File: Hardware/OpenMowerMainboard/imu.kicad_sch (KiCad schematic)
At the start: 6 parts, among them J20 Conn_01x10_Female

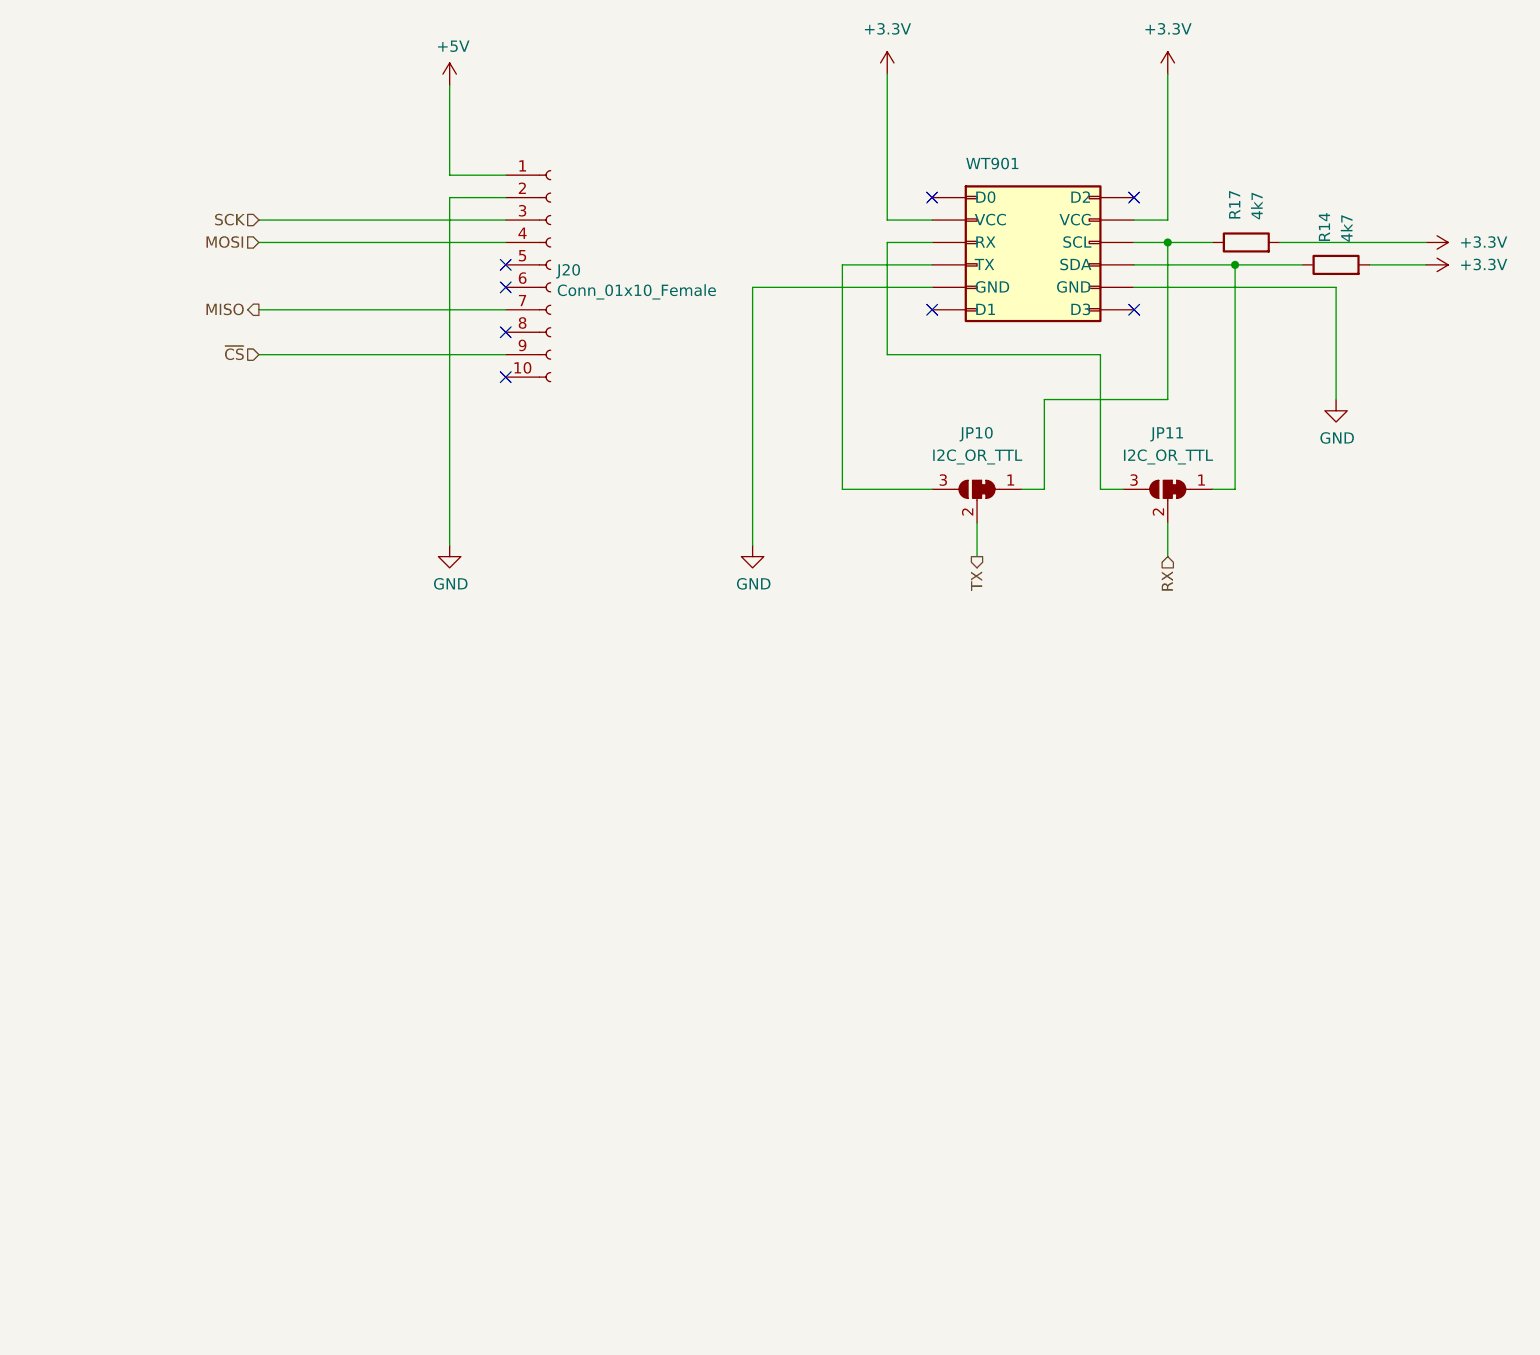
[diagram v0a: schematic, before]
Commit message: feat: added LSM6DSO as IMU
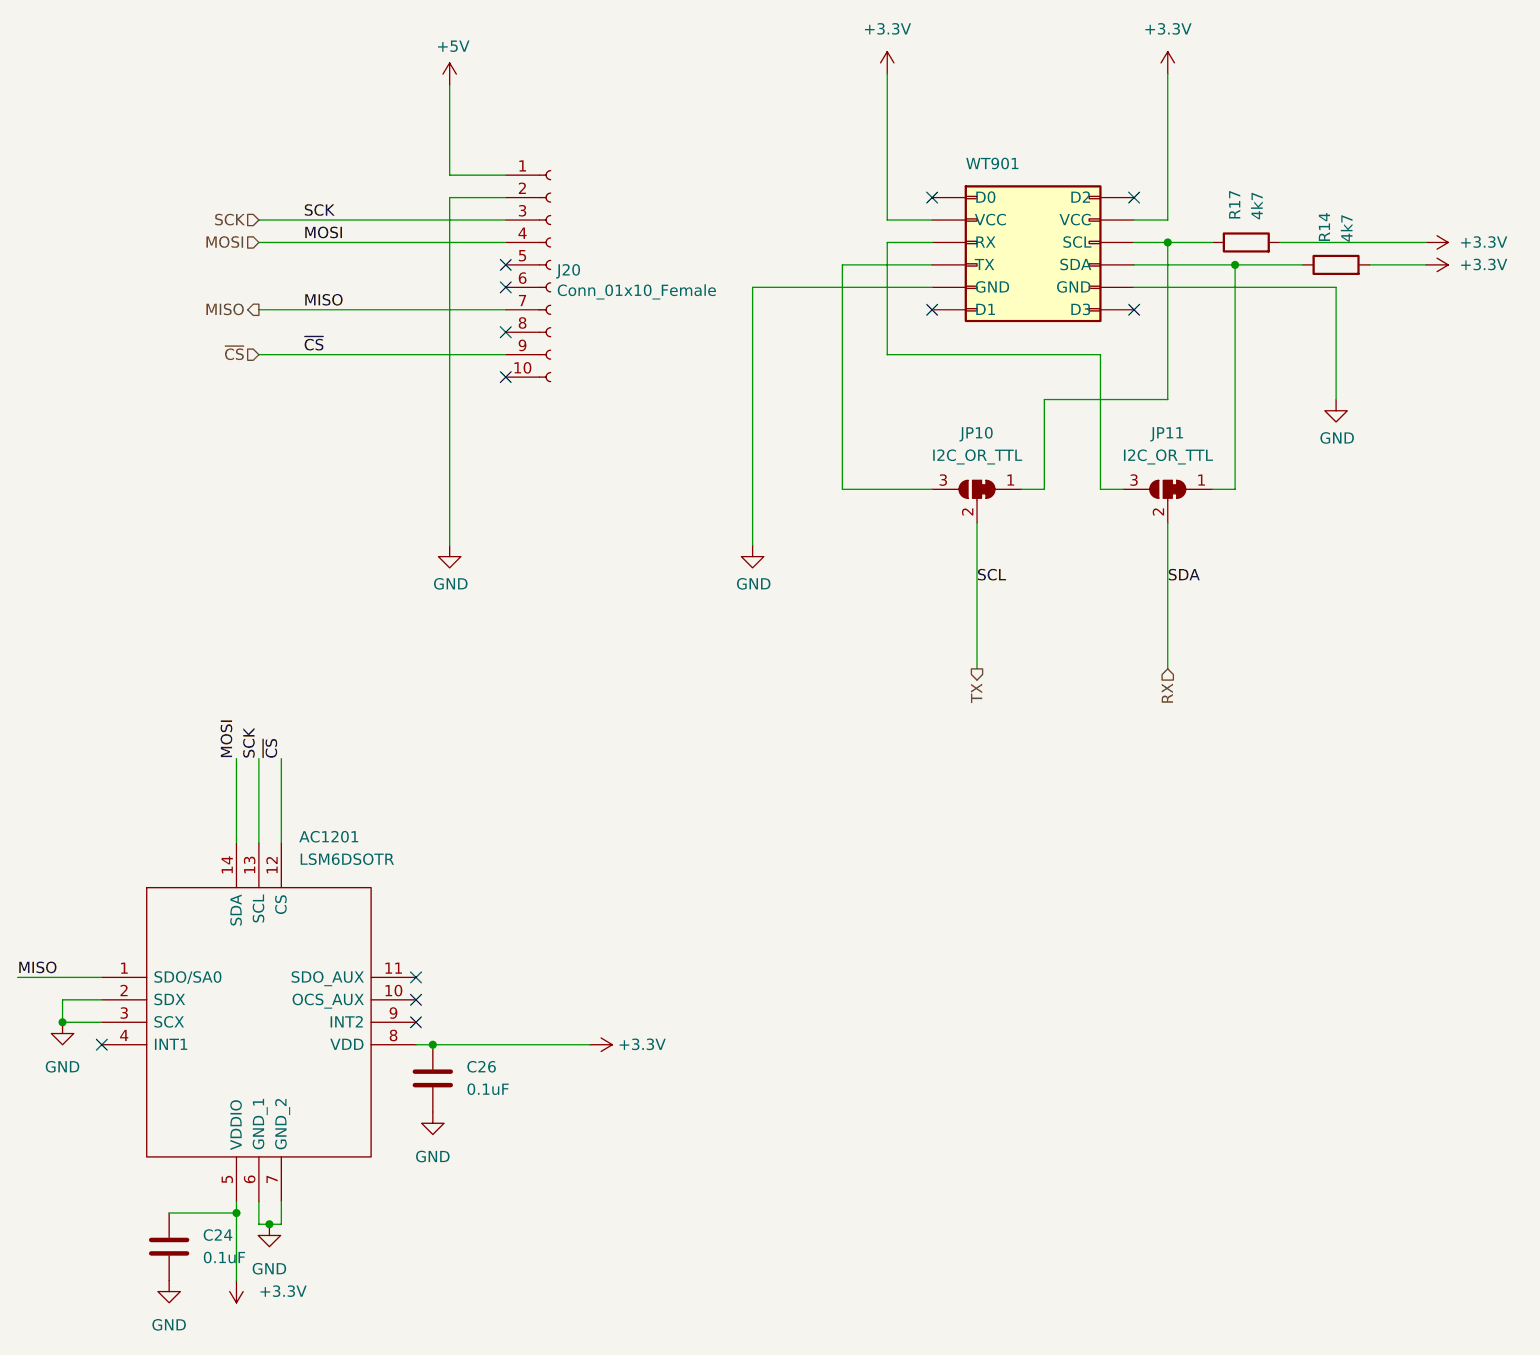
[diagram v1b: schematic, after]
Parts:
- added AC1201: LSM6DSOTR, MyModules:LGA-14_2.5X3X0.86_, symbol LSM6DSOTR:LSM6DSOTR
- added C24, C26: 0.1uF, Capacitor_SMD:C_0603_1608Metric, symbol Device:C
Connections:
- net +3V3: now also AC1201.5 (VDDIO), AC1201.8 (VDD), C24.1, C26.1
- net GND: now also AC1201.2 (SDX), AC1201.3 (SCX), AC1201.6 (GND_1), AC1201.7 (GND_2), C24.2, C26.2
- net MISO: now also AC1201.1 (SDO/SA0)
- net MOSI: now also AC1201.14 (SDA)
- net SCK: now also AC1201.13 (SCL)
- net ~{CS}: now also AC1201.12 (CS)
- no-connect marks 8 -> 12

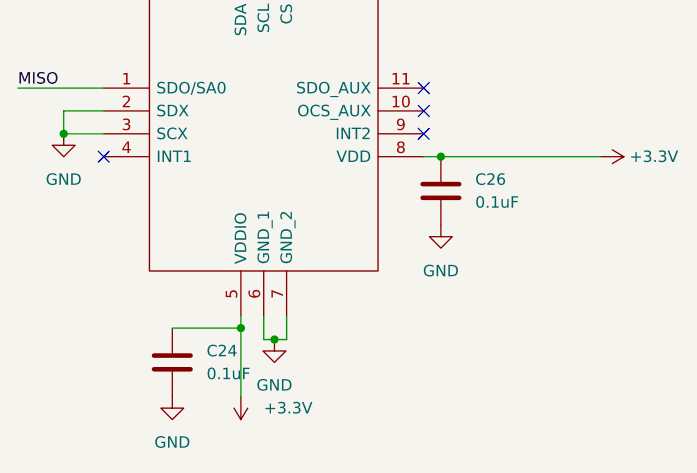
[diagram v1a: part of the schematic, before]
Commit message: chore: cleanup pcb, rearrange labels, add LCSC code
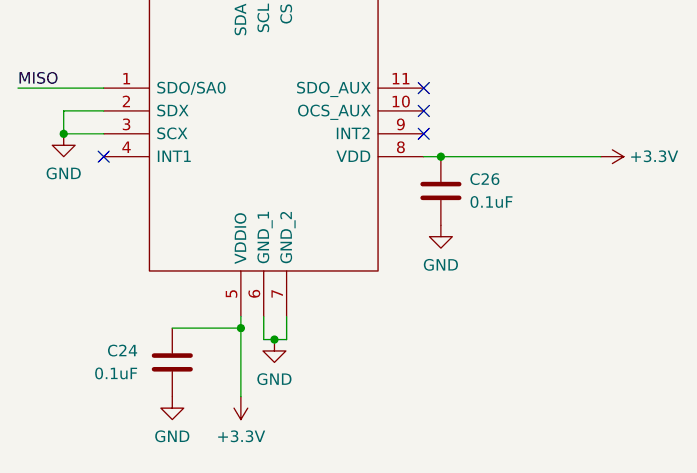
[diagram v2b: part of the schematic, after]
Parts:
- AC1201: LCSC (none) -> C2655100
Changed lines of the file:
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@@
       (effects (font (size 1.27 1.27)) hide)
     )
-    (property "Value" "GND" (id 1) (at 130.7294 179.705 0))
+    (property "Value" "GND" (id 1) (at 130.7294 179.07 0))
     (property "Footprint" "" (id 2) (at 130.7294 174.625 0)
       (effects (font (size 1.27 1.27)) hide)
@@
     )
     (property "Part Number" "LSM6DSOTR" (id 11) (at 111.76 146.685 0)
+      (effects (font (size 1.27 1.27)) hide)
+    )
+    (property "LCSC" "C2655100" (id 12) (at 111.76 146.685 0)
       (effects (font (size 1.27 1.27)) hide)
     )
@@
   (symbol (lib_id "Device:C") (at 119.38 177.165 0) (unit 1)
     (in_bom yes) (on_board yes) (fields_autoplaced)
-    (property "Reference" "C24" (id 0) (at 123.19 175.8949 0)
-      (effects (font (size 1.27 1.27)) (justify left))
-    )
-    (property "Value" "0.1uF" (id 1) (at 123.19 178.4349 0)
-      (effects (font (size 1.27 1.27)) (justify left))
+    (property "Reference" "C24" (id 0) (at 115.57 175.8949 0)
+      (effects (font (size 1.27 1.27)) (justify right))
+    )
+    (property "Value" "0.1uF" (id 1) (at 115.57 178.4349 0)
+      (effects (font (size 1.27 1.27)) (justify right))
     )
     (property "Footprint" "Capacitor_SMD:C_0603_1608Metric" (id 2) (at 120.3452 180.975 0)
@@
       (effects (font (size 1.27 1.27)) hide)
     )
-    (property "Value" "GND" (id 1) (at 119.38 186.055 0))
+    (property "Value" "GND" (id 1) (at 119.38 185.42 0))
     (property "Footprint" "" (id 2) (at 119.38 180.975 0)
       (effects (font (size 1.27 1.27)) hide)
@@
       (effects (font (size 1.27 1.27)) hide)
     )
-    (property "Value" "+3.3V" (id 1) (at 129.54 182.2449 0)
-      (effects (font (size 1.27 1.27)) (justify right))
-    )
+    (property "Value" "+3.3V" (id 1) (at 127 185.42 0))
     (property "Footprint" "" (id 2) (at 127 180.975 0)
       (effects (font (size 1.27 1.27)) hide)
@@
       (effects (font (size 1.27 1.27)) hide)
     )
-    (property "Value" "GND" (id 1) (at 149.225 167.005 0))
+    (property "Value" "GND" (id 1) (at 149.225 166.37 0))
     (property "Footprint" "" (id 2) (at 149.225 161.925 0)
       (effects (font (size 1.27 1.27)) hide)
@@
   (symbol (lib_id "Device:C") (at 149.225 158.115 0) (unit 1)
     (in_bom yes) (on_board yes) (fields_autoplaced)
-    (property "Reference" "C26" (id 0) (at 153.035 156.8449 0)
-      (effects (font (size 1.27 1.27)) (justify left))
-    )
-    (property "Value" "0.1uF" (id 1) (at 153.035 159.3849 0)
+    (property "Reference" "C26" (id 0) (at 152.4 156.8449 0)
+      (effects (font (size 1.27 1.27)) (justify left))
+    )
+    (property "Value" "0.1uF" (id 1) (at 152.4 159.3849 0)
       (effects (font (size 1.27 1.27)) (justify left))
     )
@@
       (effects (font (size 1.27 1.27)) hide)
     )
-    (property "Value" "GND" (id 1) (at 107.315 156.845 0))
+    (property "Value" "GND" (id 1) (at 107.315 156.21 0))
     (property "Footprint" "" (id 2) (at 107.315 151.765 0)
       (effects (font (size 1.27 1.27)) hide)

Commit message: feat(imu): deprecate WT901 and MPU9250 (J20)
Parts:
- J20, WT901: Config (none) -> do not place; now left out of the parts list
- JP10, JP11: now left out of the parts list
- R14, R17: Config (none) -> no not place; now left out of the parts list
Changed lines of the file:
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@@
   )
   (symbol (lib_id "Connector:Conn_01x10_Female") (at 162.56 66.04 0) (unit 1)
-    (in_bom yes) (on_board yes)
+    (in_bom no) (on_board yes)
     (property "Reference" "J20" (id 0) (at 163.2712 66.6496 0)
       (effects (font (size 1.27 1.27)) (justify left))
@@
     )
     (property "Stock_PN" "J-TH-1x10-.1" (id 6) (at 162.56 66.04 0)
+      (effects (font (size 1.27 1.27)) hide)
+    )
+    (property "Config" "do not place" (id 7) (at 162.56 66.04 0)
       (effects (font (size 1.27 1.27)) hide)
     )
@@
   )
   (symbol (lib_id "Jumper:SolderJumper_3_Bridged12") (at 232.41 91.44 0) (mirror y) (unit 1)
-    (in_bom yes) (on_board yes)
+    (in_bom no) (on_board yes)
     (property "Reference" "JP11" (id 0) (at 232.41 85.09 0))
     (property "Value" "I2C_OR_TTL" (id 1) (at 232.41 87.63 0))
@@
   )
   (symbol (lib_id "Jumper:SolderJumper_3_Bridged12") (at 210.82 91.44 0) (mirror y) (unit 1)
-    (in_bom yes) (on_board yes) (fields_autoplaced)
+    (in_bom no) (on_board yes) (fields_autoplaced)
     (property "Reference" "JP10" (id 0) (at 210.82 85.09 0))
     (property "Value" "I2C_OR_TTL" (id 1) (at 210.82 87.63 0))
@@
   )
   (symbol (lib_id "Connector_Generic:Conn_02x06_Row_Letter_First") (at 210.82 63.5 0) (unit 1)
-    (in_bom yes) (on_board yes)
+    (in_bom no) (on_board yes)
     (property "Reference" "WT901" (id 0) (at 209.55 54.61 0)
       (effects (font (size 1.27 1.27)) (justify left))
@@
     )
     (property "Datasheet" "~" (id 3) (at 210.82 63.5 0)
+      (effects (font (size 1.27 1.27)) hide)
+    )
+    (property "Config" "do not place" (id 4) (at 210.82 63.5 0)
       (effects (font (size 1.27 1.27)) hide)
     )
@@
   )
   (symbol (lib_id "Device:R") (at 251.46 66.04 90) (unit 1)
-    (in_bom yes) (on_board yes) (fields_autoplaced)
+    (in_bom no) (on_board yes) (fields_autoplaced)
     (property "Reference" "R14" (id 0) (at 250.1899 63.5 0)
       (effects (font (size 1.27 1.27)) (justify left))
@@
     )
     (property "Datasheet" "~" (id 3) (at 251.46 66.04 0)
+      (effects (font (size 1.27 1.27)) hide)
+    )
+    (property "Config" "no not place" (id 4) (at 251.46 66.04 0)
       (effects (font (size 1.27 1.27)) hide)
     )
@@
   )
   (symbol (lib_id "Device:R") (at 241.3 63.5 90) (unit 1)
-    (in_bom yes) (on_board yes) (fields_autoplaced)
+    (in_bom no) (on_board yes) (fields_autoplaced)
     (property "Reference" "R17" (id 0) (at 240.0299 60.96 0)
       (effects (font (size 1.27 1.27)) (justify left))
@@
       (effects (font (size 1.27 1.27)) hide)
     )
+    (property "Config" "no not place" (id 4) (at 241.3 63.5 0)
+      (effects (font (size 1.27 1.27)) hide)
+    )

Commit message: feat(bom): update LCSC codes
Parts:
- C24, C26: LCSC (none) -> C15725
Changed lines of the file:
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@@
+      (effects (font (size 1.27 1.27)) hide)
+    )
+    (property "LCSC" "C15725" (id 7) (at 119.38 177.165 0)
       (effects (font (size 1.27 1.27)) hide)
     )
@@
       (effects (font (size 1.27 1.27)) hide)
     )
+    (property "LCSC" "C15725" (id 7) (at 149.225 158.115 0)
+      (effects (font (size 1.27 1.27)) hide)
+    )
